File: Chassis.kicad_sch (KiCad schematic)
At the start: 53 parts, among them J1 FR_JST, J10 IN_XT30, J11 SWD_IN, J12 Conn_01x08_Pin, J13 GIM1_JST, J14 GIM2_JST, J15 GIM1_XT30, J16 GIM2_XT30, J17 SWD_OUT, J18 CHA_XT30, J19 SHOO_XT30, J2 BR_JST, J20 GIM_XT30, J21 OUT_JST, J22 5V_XT30, J23 UART_IN, J24 UART_Out, J25 REF_IN, J26 REF_OUT, J27 CAN2_IN, J28 CAN2_OUT, J29 Conn_01x04_Pin, J3 FL_JST, J30 Conn_01x04_Pin, J31 Conn_01x04_Pin, J32 BR_XT30, J33 BR_XT30, J4 BL_JST, J5 FR_XT30, J6 BR_XT30, J7 FL_XT30, J8 BL_XT30, J9 IN_JST

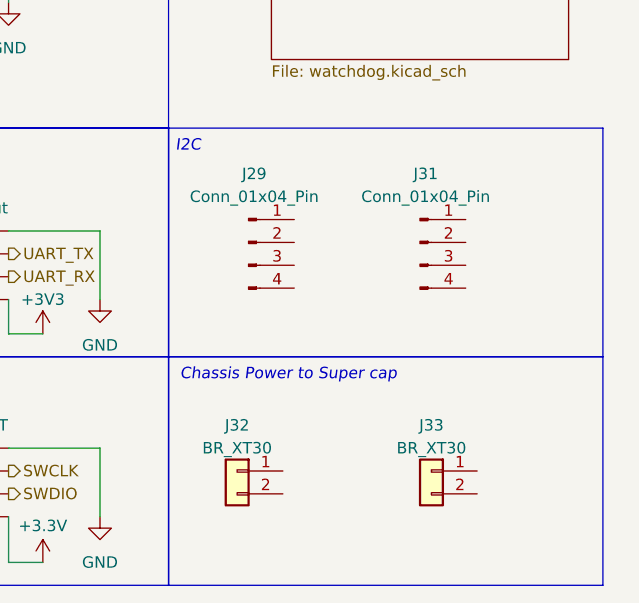
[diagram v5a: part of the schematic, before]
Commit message: added connections for chassis power to supercap
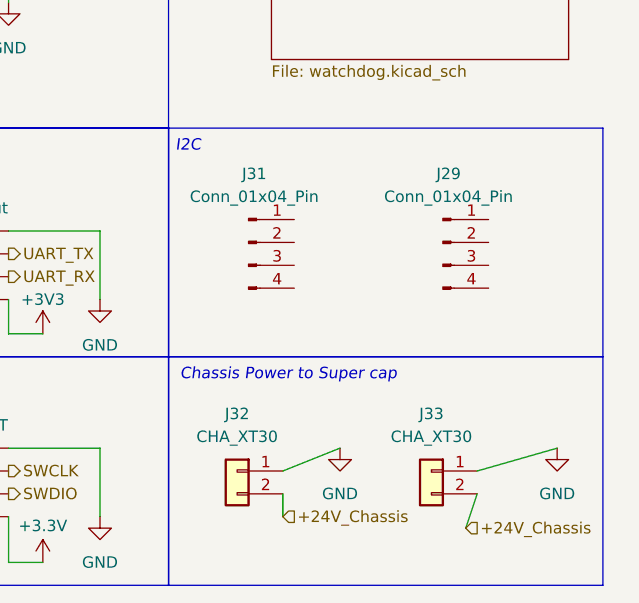
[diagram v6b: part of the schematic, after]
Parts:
- J32, J33: value BR_XT30 -> CHA_XT30
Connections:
- net +24V_BL_ESC: now also J32.2 (Pin_2), J33.2 (Pin_2)
- net GND: now also J32.1 (Pin_1), J33.1 (Pin_1)
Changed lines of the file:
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@@
 	(wire
 		(pts
+			(xy 269.24 153.67) (xy 267.97 157.48)
+		)
+		(stroke
+			(width 0)
+			(type default)
+		)
+	)
+	(wire
+		(pts
 			(xy 219.71 67.31) (xy 218.44 67.31)
 		)
@@
 	(wire
 		(pts
+			(xy 247.65 151.13) (xy 254 148.59)
+		)
+		(stroke
+			(width 0)
+			(type default)
+		)
+	)
+	(wire
+		(pts
 			(xy 39.37 74.93) (xy 38.1 74.93)
 		)
@@
 		)
 	)
+	(wire
+		(pts
+			(xy 269.24 151.13) (xy 278.13 148.59)
+		)
+		(stroke
+			(width 0)
+			(type default)
+		)
+	)
 	(polyline
 		(pts
@@
 	(wire
 		(pts
+			(xy 247.65 153.67) (xy 247.65 156.21)
+		)
+		(stroke
+			(width 0)
+			(type default)
+		)
+	)
+	(wire
+		(pts
 			(xy 196.85 161.29) (xy 200.66 161.29)
 		)
@@
 		)
 	)
+	(hierarchical_label "+24V_Chassis"
+		(shape input)
+		(at 247.65 156.21 0)
+		(fields_autoplaced yes)
+		(effects
+			(font
+				(size 1.27 1.27)
+			)
+			(justify left)
+		)
+	)
 	(hierarchical_label "+24V_FL_ESC"
 		(shape output)
@@
 		)
 	)
+	(hierarchical_label "+24V_Chassis"
+		(shape input)
+		(at 267.97 157.48 0)
+		(fields_autoplaced yes)
+		(effects
+			(font
+				(size 1.27 1.27)
+			)
+			(justify left)
+		)
+	)
 	(hierarchical_label "CAN-_BR_ESC"
 		(shape output)
@@
 	(symbol
 		(lib_id "Connector:Conn_01x04_Pin")
-		(at 243.84 125.73 0)
+		(at 265.43 125.73 0)
 		(unit 1)
 		(exclude_from_sim no)
@@
 		(on_board yes)
 		(dnp no)
-		(fields_autoplaced yes)
 		(property "Reference" "J29"
-			(at 244.475 118.11 0)
+			(at 266.065 118.11 0)
 			(effects
 				(font
@@
 		)
 		(property "Value" "Conn_01x04_Pin"
-			(at 244.475 120.65 0)
+			(at 266.065 120.65 0)
 			(effects
 				(font
@@
 		)
 		(property "Footprint" ""
-			(at 243.84 125.73 0)
+			(at 265.43 125.73 0)
 			(effects
 				(font
@@
 		)
 		(property "Datasheet" "~"
-			(at 243.84 125.73 0)
+			(at 265.43 125.73 0)
 			(effects
 				(font
@@
 		)
 		(property "Description" "Generic connector, single row, 01x04, script generated"
-			(at 243.84 125.73 0)
+			(at 265.43 125.73 0)
 			(effects
 				(font
@@
 			)
 		)
+		(pin "2"
+		)
 		(pin "3"
 		)
 		(pin "1"
 		)
-		(pin "2"
-		)
 		(pin "4"
 		)
@@
 	)
 	(symbol
-		(lib_id "Connector:Conn_01x04_Pin")
-		(at 262.89 125.73 0)
-		(unit 1)
-		(exclude_from_sim no)
-		(in_bom yes)
-		(on_board yes)
-		(dnp no)
-		(fields_autoplaced yes)
-		(property "Reference" "J31"
-			(at 263.525 118.11 0)
-			(effects
-				(font
-					(size 1.27 1.27)
-				)
-			)
-		)
-		(property "Value" "Conn_01x04_Pin"
-			(at 263.525 120.65 0)
-			(effects
-				(font
-					(size 1.27 1.27)
-				)
-			)
-		)
-		(property "Footprint" ""
-			(at 262.89 125.73 0)
-			(effects
-				(font
-					(size 1.27 1.27)
-				)
-				(hide yes)
-			)
-		)
-		(property "Datasheet" "~"
-			(at 262.89 125.73 0)
-			(effects
-				(font
-					(size 1.27 1.27)
-				)
-				(hide yes)
-			)
-		)
-		(property "Description" "Generic connector, single row, 01x04, script generated"
-			(at 262.89 125.73 0)
-			(effects
-				(font
-					(size 1.27 1.27)
-				)
-				(hide yes)
-			)
-		)
-		(pin "1"
-		)
-		(pin "4"
-		)
-		(pin "2"
-		)
-		(pin "3"
-		)
-		(instances
-			(project ""
-				(path "/d5f28ba3-2393-441a-9a3a-5aa9d797472a"
-					(reference "J31")
-					(unit 1)
-				)
-			)
-		)
-	)
-	(symbol
 		(lib_id "power:GND")
 		(at 113.03 148.59 0)
@@
 		(fields_autoplaced yes)
 		(property "Reference" "J33"
-			(at 264.16 146.05 0)
+			(at 264.16 144.78 0)
 			(effects
 				(font
@@
 			)
 		)
-		(property "Value" "BR_XT30"
-			(at 264.16 148.59 0)
+		(property "Value" "CHA_XT30"
+			(at 264.16 147.32 0)
 			(effects
 				(font
@@
 	)
 	(symbol
+		(lib_id "Connector:Conn_01x04_Pin")
+		(at 243.84 125.73 0)
+		(unit 1)
+		(exclude_from_sim no)
+		(in_bom yes)
+		(on_board yes)
+		(dnp no)
+		(property "Reference" "J31"
+			(at 244.475 118.11 0)
+			(effects
+				(font
+					(size 1.27 1.27)
+				)
+			)
+		)
+		(property "Value" "Conn_01x04_Pin"
+			(at 244.475 120.65 0)
+			(effects
+				(font
+					(size 1.27 1.27)
+				)
+			)
+		)
+		(property "Footprint" ""
+			(at 243.84 125.73 0)
+			(effects
+				(font
+					(size 1.27 1.27)
+				)
+				(hide yes)
+			)
+		)
+		(property "Datasheet" "~"
+			(at 243.84 125.73 0)
+			(effects
+				(font
+					(size 1.27 1.27)
+				)
+				(hide yes)
+			)
+		)
+		(property "Description" "Generic connector, single row, 01x04, script generated"
+			(at 243.84 125.73 0)
+			(effects
+				(font
+					(size 1.27 1.27)
+				)
+				(hide yes)
+			)
+		)
+		(pin "2"
+		)
+		(pin "3"
+		)
+		(pin "1"
+		)
+		(pin "4"
+		)
+		(instances
+			(project "Chassis"
+				(path "/d5f28ba3-2393-441a-9a3a-5aa9d797472a"
+					(reference "J31")
+					(unit 1)
+				)
+			)
+		)
+	)
+	(symbol
 		(lib_id "power:GND1")
 		(at 199.39 48.26 0)
@@
 		(fields_autoplaced yes)
 		(property "Reference" "J32"
-			(at 242.57 146.05 0)
+			(at 242.57 144.78 0)
 			(effects
 				(font
@@
 			)
 		)
-		(property "Value" "BR_XT30"
-			(at 242.57 148.59 0)
+		(property "Value" "CHA_XT30"
+			(at 242.57 147.32 0)
 			(effects
 				(font
@@
 	(symbol
 		(lib_id "power:GND")
+		(at 278.13 148.59 0)
+		(unit 1)
+		(exclude_from_sim no)
+		(in_bom yes)
+		(on_board yes)
+		(dnp no)
+		(fields_autoplaced yes)
+		(property "Reference" "#PWR050"
+			(at 278.13 154.94 0)
+			(effects
+				(font
+					(size 1.27 1.27)
+				)
+				(hide yes)
+			)
+		)
+		(property "Value" "GND"
+			(at 278.13 153.67 0)
+			(effects
+				(font
+					(size 1.27 1.27)
+				)
+			)
+		)
+		(property "Footprint" ""
+			(at 278.13 148.59 0)
+			(effects
+				(font
+					(size 1.27 1.27)
+				)
+				(hide yes)
+			)
+		)
+		(property "Datasheet" ""
+			(at 278.13 148.59 0)
+			(effects
+				(font
+					(size 1.27 1.27)
+				)
+				(hide yes)
+			)
+		)
+		(property "Description" ""
+			(at 278.13 148.59 0)
+			(effects
+				(font
+					(size 1.27 1.27)
+				)
+				(hide yes)
+			)
+		)
+		(pin "1"
+		)
+		(instances
+			(project "Chassis"
+				(path "/d5f28ba3-2393-441a-9a3a-5aa9d797472a"
+					(reference "#PWR050")
+					(unit 1)
+				)
+			)
+		)
+	)
+	(symbol
+		(lib_id "power:GND")
 		(at 67.31 128.27 0)
 		(unit 1)
@@
 					(unit 1)
 				)
+			)
+		)
+	)
+	(symbol
+		(lib_id "power:GND")
+		(at 254 148.59 0)
+		(unit 1)
+		(exclude_from_sim no)
+		(in_bom yes)
+		(on_board yes)
+		(dnp no)
+		(fields_autoplaced yes)
+		(property "Reference" "#PWR049"
+			(at 254 154.94 0)
+			(effects
+				(font
+					(size 1.27 1.27)
+				)
+				(hide yes)
+			)
+		)
+		(property "Value" "GND"
+			(at 254 153.67 0)
+			(effects
+				(font
+					(size 1.27 1.27)
+				)
+			)
+		)
+		(property "Footprint" ""
+			(at 254 148.59 0)
+			(effects
+				(font
+					(size 1.27 1.27)
+				)
+				(hide yes)
+			)
+		)
+		(property "Datasheet" ""
+			(at 254 148.59 0)
+			(effects
+				(font
+					(size 1.27 1.27)
+				)
+				(hide yes)
+			)
+		)
+		(property "Description" ""
+			(at 254 148.59 0)
+			(effects
+				(font
+					(size 1.27 1.27)
+				)
+				(hide yes)
+			)
+		)
+		(pin "1"
+		)
+		(instances
+			(project "Chassis"
+				(path "/d5f28ba3-2393-441a-9a3a-5aa9d797472a"
+					(reference "#PWR049")
+					(unit 1)
+				)

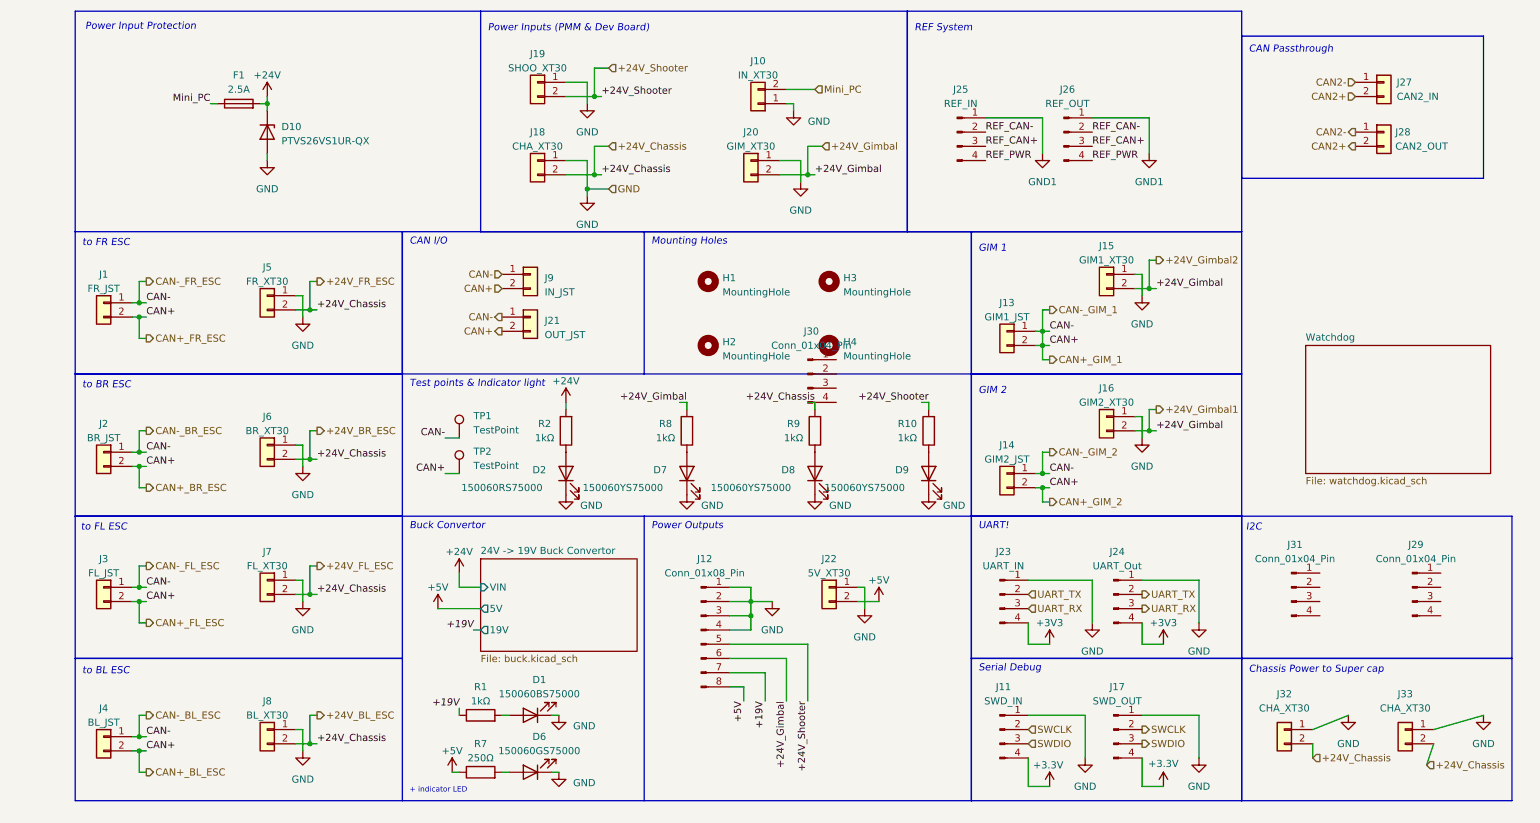
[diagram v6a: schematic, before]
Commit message: Added hierarchical labels to ground pins in chassis
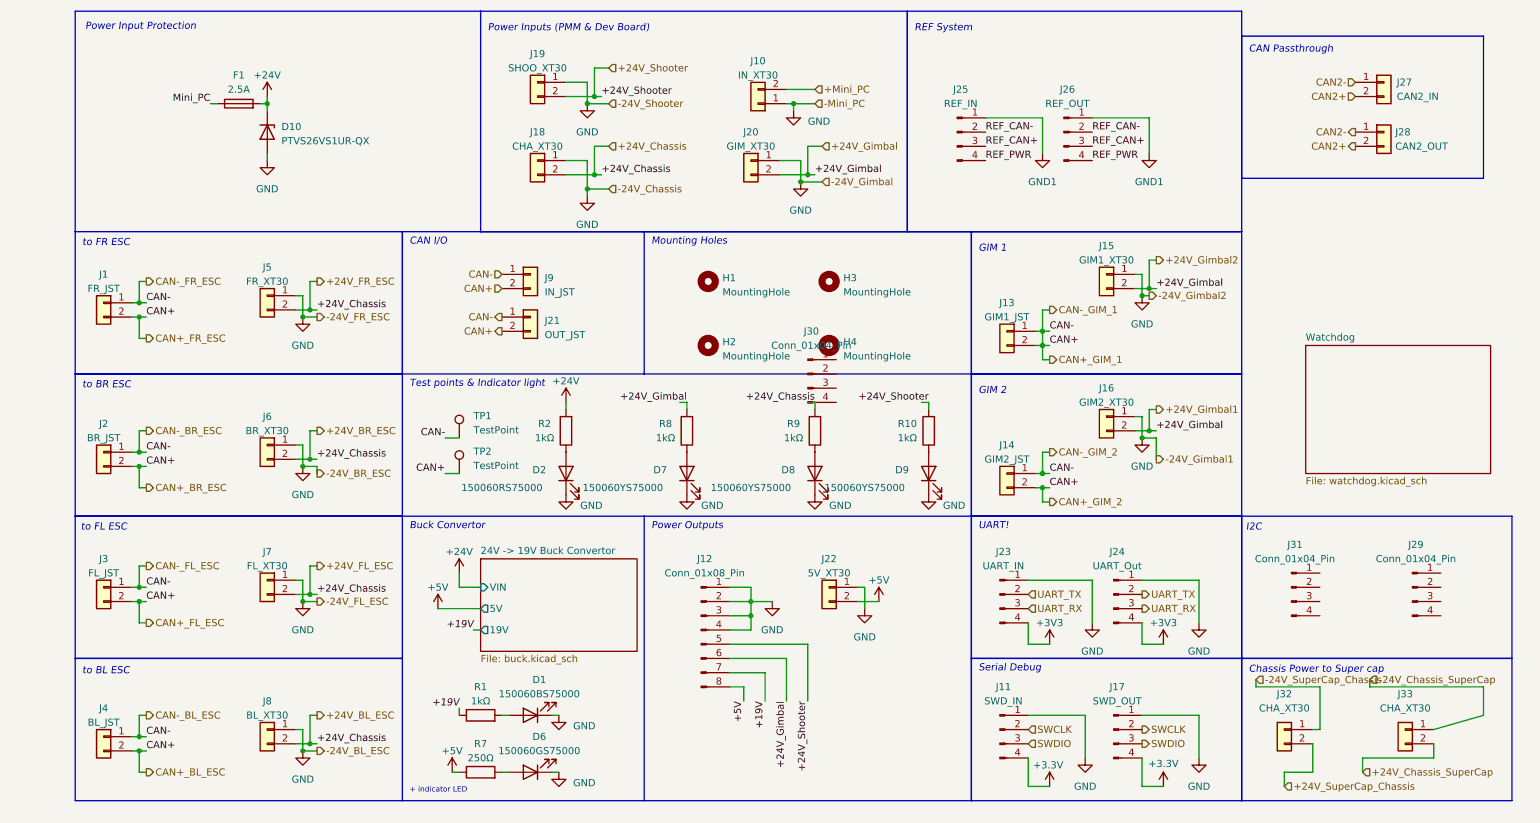
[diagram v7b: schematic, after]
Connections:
- net +24V_BL_ESC: no longer J32.2 (Pin_2), J33.2 (Pin_2)
- net GND: no longer J32.1 (Pin_1), J33.1 (Pin_1)
- net Mini_PC: no longer J10.2 (Pin_2)
- new net +24V_Chassis_SuperCap: J33.2 (Pin_2)
- new net +24V_SuperCap_Chassis: J32.2 (Pin_2)
- new net +Mini_PC: J10.2 (Pin_2)
- new net -24V_Chassis_SuperCap: J33.1 (Pin_1)
- new net -24V_SuperCap_Chassis: J32.1 (Pin_1)

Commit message: added supercap connection
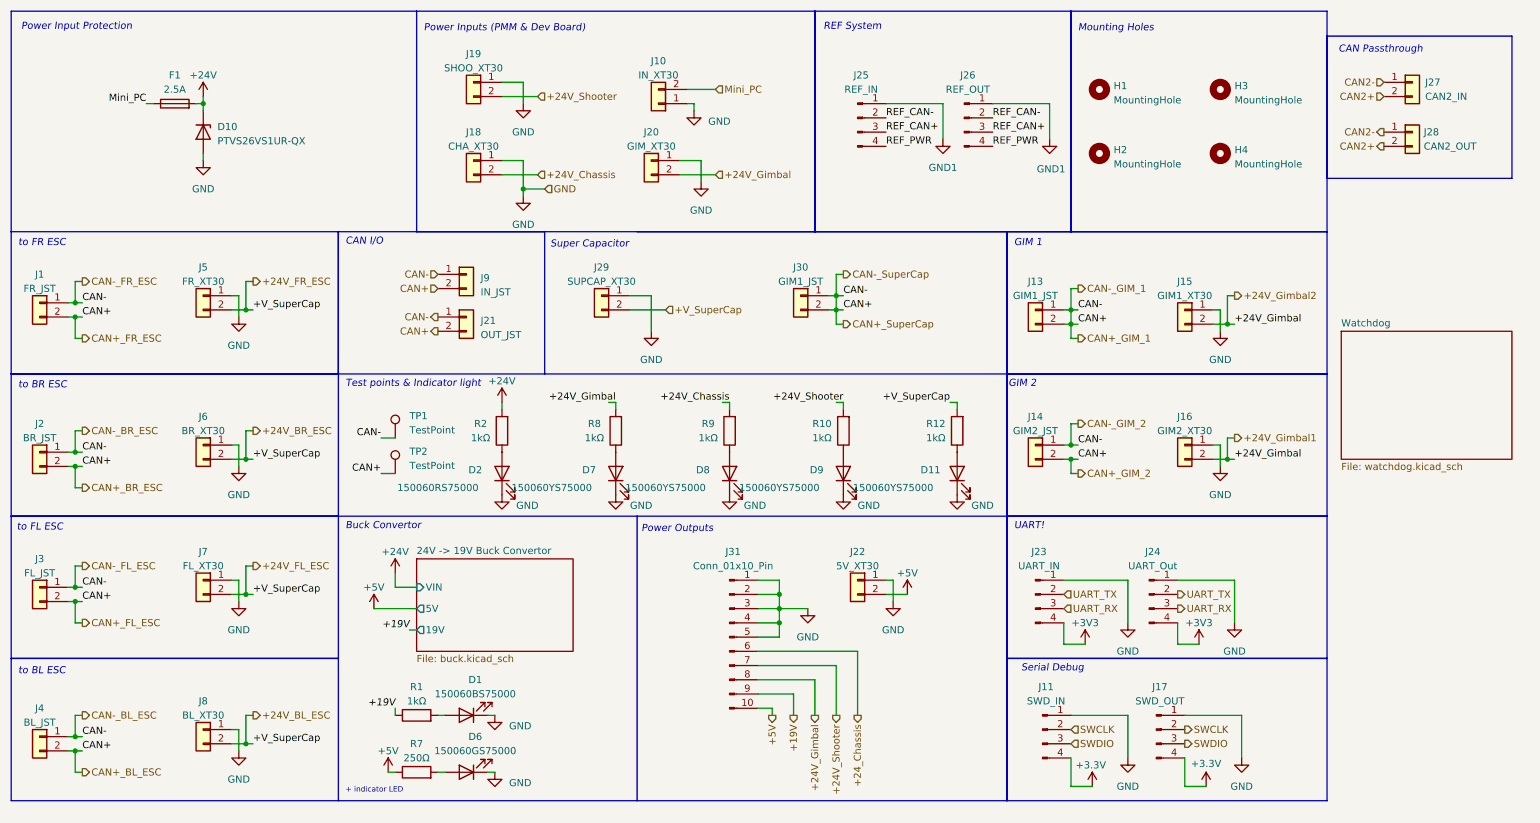
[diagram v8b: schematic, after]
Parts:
- removed J12: Conn_01x08_Pin, Robomaster_Connectors:CON_1722981108_MOL, symbol Connector:Conn_01x08_Pin
- removed J29, J30, J31: Conn_01x04_Pin, symbol Connector:Conn_01x04_Pin
- removed J32, J33: CHA_XT30, Robomaster_Connectors:AMASS_XT30U-F_1x02_P5.0mm_Vertical, symbol Connector_Generic:Conn_01x02
- added D11: 150060YS75000, LED_SMD:LED_0603_1608Metric_Pad1.05x0.95mm_HandSolder, symbol Device:LED
- added J29: SUPCAP_XT30, Robomaster_Connectors:AMASS_XT30U-F_1x02_P5.0mm_Vertical, symbol Connector_Generic:Conn_01x02
- added J30: GIM1_JST, Connector_JST:JST_GH_BM02B-GHS-TBT_1x02-1MP_P1.25mm_Vertical, symbol Connector_Generic:Conn_01x02
- added J31: Conn_01x10_Pin, symbol Connector:Conn_01x10_Pin
- added R12: 1kΩ, Resistor_SMD:R_0603_1608Metric_Pad0.98x0.95mm_HandSolder, symbol Device:R
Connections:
- net +Mini_PC is gone; now on net Mini_PC: J10.2 (Pin_2)
- net +19V: now also J31.9 (Pin_9)
- net +24V_BL_ESC: now also J29.2 (Pin_2), R12.2; no longer J18.2 (Pin_2), R9.2
- net +24V_Gimbal: now also J31.8 (Pin_8)
- net +24V_Shooter: now also J31.7 (Pin_7)
- net +5V: now also J31.10 (Pin_10)
- net CAN+: now also J30.1 (Pin_1), J30.2 (Pin_2)
- net GND: now also D11.1 (K), J29.1 (Pin_1), J31.1 (Pin_1), J31.2 (Pin_2), J31.3 (Pin_3), J31.4 (Pin_4), J31.5 (Pin_5)
- new net: D11.2 (A), R12.1
- new net +24V_Chassis: J18.2 (Pin_2), R9.2
- new net +24_Chassis: J31.6 (Pin_6)
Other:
- note added: "Super Capacitor"
- note removed: "Chassis Power to Super cap"
- note removed: "I2C"
- moved on the sheet: D1, D10, D2, D6, D7, D8, D9, F1, H1, H2, H3, H4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
